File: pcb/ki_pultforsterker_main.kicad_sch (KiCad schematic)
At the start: 256 parts, among them J1 24V IN, J10 LED-RINGER, J11 USB-C 16P, J12 USB-C 16P, J13 TFT, J15 USB1, J16 USB2, J17 USB3, J18 USB4, J19 USB PI, J2 SPK L, J20 AUX2, J21 PWR BAK, J22 EXP, J23 HODETLF, J24 NTC, J3 SPK R, J4 AUX1, J5 RPi 40-pin, J6 5V -> PI, J7 KNAPPER, J8 ENCODER, J9 OLED, K1 SRD-05VDC-SL-C, Q10 AO3401A, Q11 AOD409, Q2 AO3400A, Q3 AO3400A, Q4 AO3400A, Q5 AO3400A, Q6 AO3400A, Q7 AO3400A, Q8 AO3401A, Q9 AO3400A, U1 TPS54560DDAR, U10 PCM1808PWR, U11 PCM2900CDB, U12 MCP23017-E/SS, U13 TPA6132A2RTER, U14 SN74LVC1G14DBVR, U2 AMS1117-3.3, U3 LM2662MX, U4 PCM5102APWR, U5 PGA2311UA, U6 TPA3116D2DADR, U7 FE1.1s, U8 TS3USB221RSER, U9 AMS1117-3.3, X1 12.288MHz, Y1 12MHz, Y2 12MHz

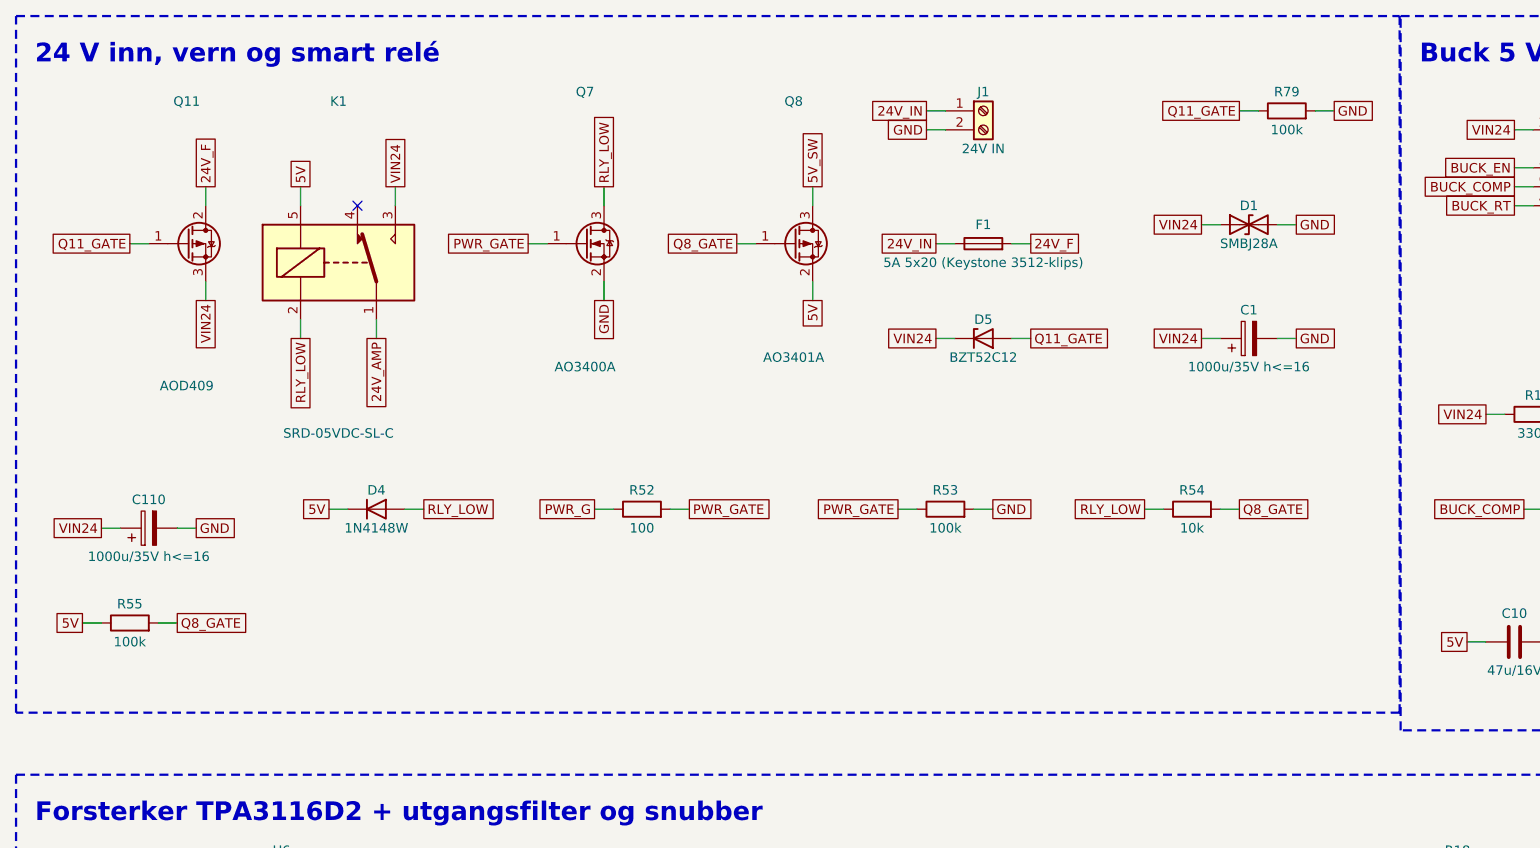
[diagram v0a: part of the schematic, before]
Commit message: PCB rev B: produksjonsfiler med Littelfuse 111-sikringsklips (F1) – DRC ren; skjema regenerert
Co-Authored-By: Claude Fable 5.1 <noreply@anthropic.com>
Claude-Session: https://claude.ai/code/session_01FaJKmYinw8SWRobKXBRYpt
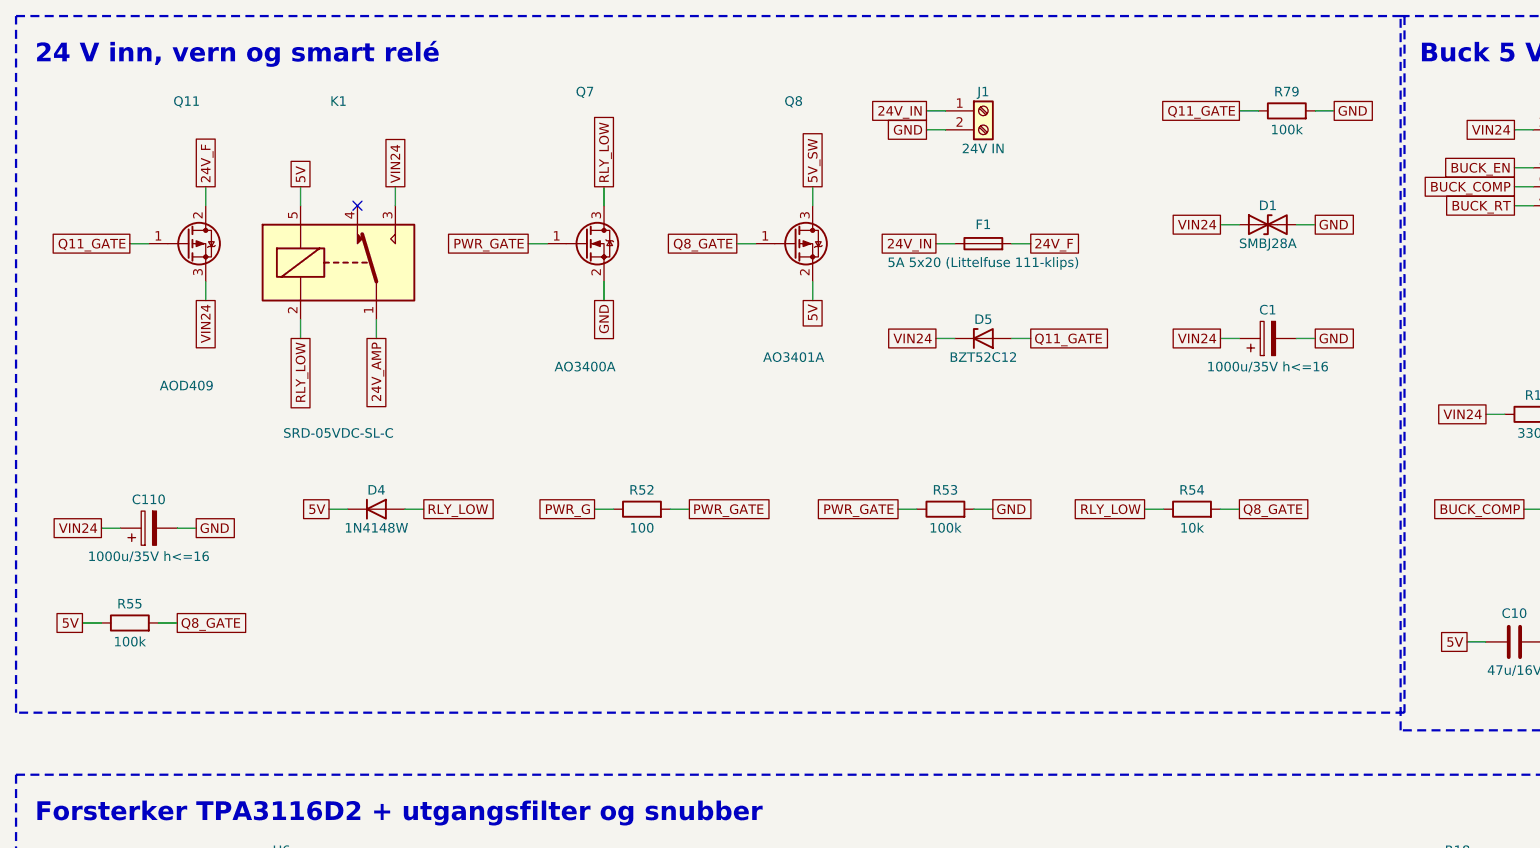
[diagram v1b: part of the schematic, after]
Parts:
- F1: value 5A 5x20 (Keystone 3512-klips) -> 5A 5x20 (Littelfuse 111-klips); footprint Fuse:Fuseholder_Clip-5x20mm_Keystone_3512P_Inline_P23.62x7.27mm_D1.02x2.41x1.02x1.57mm_Horizontal -> Fuse:Fuseholder_Clip-5x20mm_Littelfuse_111_Inline_P20.00x5.00mm_D1.05mm_Horizontal; LCSC (none) -> C151075

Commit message: PCB: skjema regenerert med nye footprints (U1/U7/U8) og rettet U4 – 0 avvik mot kortet
Co-Authored-By: Claude Opus 5.5 <noreply@anthropic.com>
Claude-Session: https://claude.ai/code/session_01FaJKmYinw8SWRobKXBRYpt
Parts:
- C1, C110: value 1000u/35V h<=16 -> 680-1000u/35V 10x16
- U1: footprint Package_SO:HSOP-8-1EP_3.9x4.9mm_P1.27mm_EP2.3x2.3mm -> Package_SO:Texas_HSOP-8-1EP_3.9x4.9mm_P1.27mm
- U7: footprint Package_SO:SSOP-28_5.3x10.2mm_P0.65mm -> Package_SO:SSOP-28_3.9x9.9mm_P0.635mm; Beskrivelse USB 2.0 4-ports hub -> USB 2.0 4-ports hub – FE1.1S-BSOP28 er SSOP-28 150 mil (3,9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
- U8: footprint Package_DFN_QFN:UQFN-10_1.4x1.8mm_P0.4mm -> Package_DFN_QFN:Texas_UQFN-10_1.5x2mm_P0.5mm
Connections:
- net DAC_LDOO: now also U4.18 (LDOO); no longer U4.10 (DEMP)
- net GND: now also U4.10 (DEMP); no longer U4.18 (LDOO)
